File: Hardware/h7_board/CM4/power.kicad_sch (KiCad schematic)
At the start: 26 parts, among them IC4 TPS65133DPDR, IC5 TPS62111RSAT, J2 USB_C_Receptacle_USB2.0, Q1 AO3401A, U1 USBLC6-2SC6, U3 REF3433IDBVR

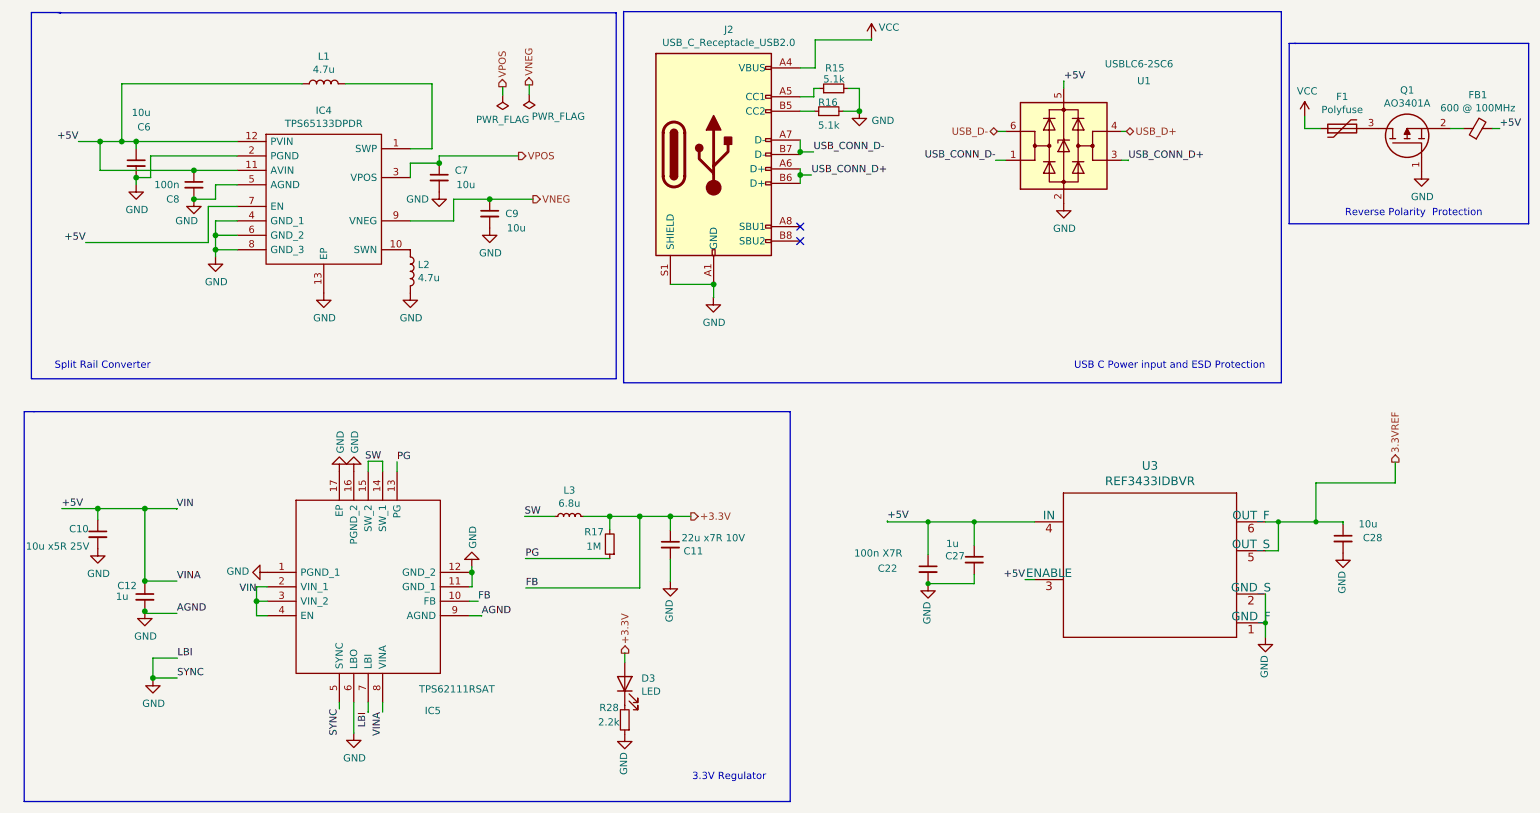
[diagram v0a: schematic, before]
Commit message: Edited Design to modify to LDO regulator and improve board layout
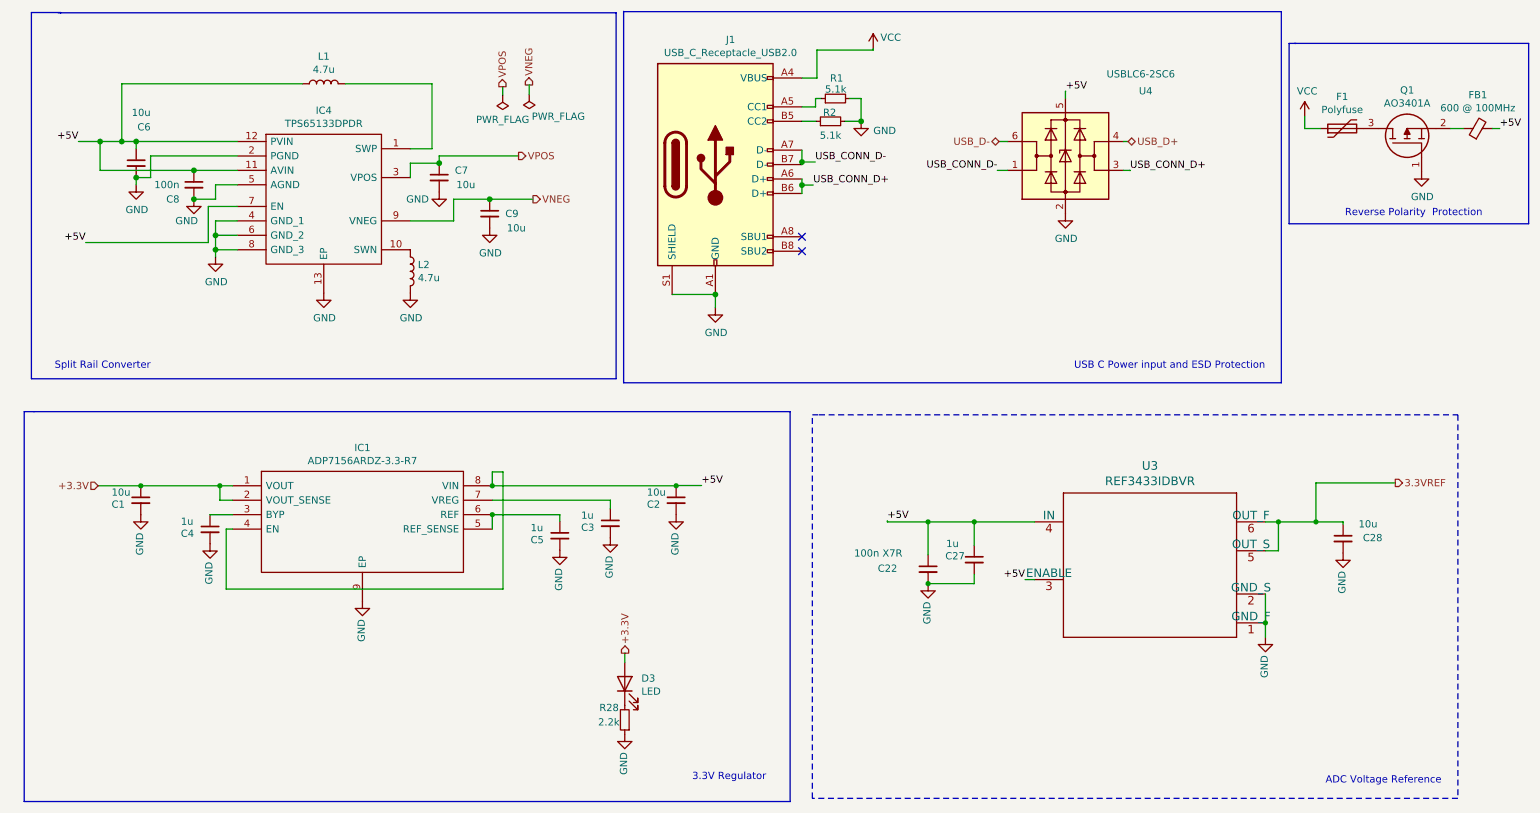
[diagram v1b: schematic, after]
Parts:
- removed C10: 10u x5R 25V, Capacitor_SMD:C_1210_3225Metric, symbol Device:C_Small
- removed C11: 22u x7R 10V, Capacitor_SMD:C_1210_3225Metric, symbol Device:C_Small
- removed C12: 1u, Capacitor_SMD:C_0805_2012Metric, symbol Device:C_Small
- removed IC5: TPS62111RSAT, SamacSys_Parts:QFN65P400X400X100-17N-D, symbol SamacSys_Parts:TPS62111RSAT
- removed J2: USB_C_Receptacle_USB2.0, CM4IO:TYPE-C-31-M-12, symbol Connector:USB_C_Receptacle_USB2.0
- removed L3: 6.8u, Inductor_SMD:L_TDK_SLF7032, symbol Device:L_Small
- removed R15, R16: 5.1k, Resistor_SMD:R_1206_3216Metric, symbol Device:R_Small
- removed R17: 1M, Resistor_SMD:R_0805_2012Metric, symbol Device:R_Small
- removed U1: USBLC6-2SC6, Package_TO_SOT_SMD:SOT-23-6, symbol Power_Protection:USBLC6-2SC6
- removed U3: REF3433IDBVR, footprints:REF3433IDBVR, symbol 2020-12-07_21-32-03:REF3433IDBVR
- added C1, C2: 10u, Capacitor_SMD:C_0603_1608Metric, symbol Device:C_Small
- added C3, C4, C5: 1u, Capacitor_SMD:C_0603_1608Metric, symbol Device:C_Small
- added IC1: ADP7156ARDZ-3.3-R7, SamacSys_Parts:SOIC127P600X175-9N, symbol SamacSys_Parts:ADP7156ARDZ-3.3-R7
- added J1: USB_C_Receptacle_USB2.0, CM4IO:TYPE-C-31-M-12, symbol Connector:USB_C_Receptacle_USB2.0
- added R1, R2: 5.1k, Resistor_SMD:R_1206_3216Metric, symbol Device:R_Small
- added U3: REF3433IDBVR, REF3433:REF3433IDBVR, symbol REF3433DBVR:REF3433IDBVR
- added U4: USBLC6-2SC6, Package_TO_SOT_SMD:SOT-23-6, symbol Power_Protection:USBLC6-2SC6
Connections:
- net +3.3V: now also C1.1, IC1.1 (VOUT), IC1.2 (VOUT_SENSE)
- net +5V: now also C2.1, IC1.4 (EN), IC1.8 (VIN), U3.3 (ENABLE), U3.4 (IN), U4.5 (VBUS)
- net 3.3VREF: now also U3.5 (OUT_S), U3.6 (OUT_F)
- net GND: now also C1.2, C2.2, C3.2, C4.2, C5.2, IC1.9 (EP), J1.A1 (GND), J1.A12 (GND), J1.B1 (GND), J1.B12 (GND), J1.S1 (SHIELD), R1.2, R2.2, U3.1 (GND_F), U3.2 (GND_S), U4.2 (GND)
- net USB_CONN_D+: now also J1.A6 (D+), J1.B6 (D+), U4.3 (I/O2)
- net USB_CONN_D-: now also J1.A7 (D-), J1.B7 (D-), U4.1 (I/O1)
- net USB_D+: now also U4.4 (I/O2)
- net USB_D-: now also U4.6 (I/O1)
- net VCC: now also J1.A4 (VBUS), J1.A9 (VBUS), J1.B4 (VBUS), J1.B9 (VBUS)
- new net: C3.1, IC1.7 (VREG)
- new net: J1.A5 (CC1), R1.1
- new net: C5.1, IC1.5 (REF_SENSE), IC1.6 (REF)
- new net: J1.B5 (CC2), R2.1
- new net: C4.1, IC1.3 (BYP)
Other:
- note added: "ADC Voltage Reference"

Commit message: Added Low noise analysis and design files
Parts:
- C1, C2: LCSC Part # C15849 -> C19702
- J1: LCSC Part # (none) -> C165948
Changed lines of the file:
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@@
   (junction (at 237.0328 103.7844) (diameter 0.9144) (color 0 0 0 0))
   (junction (at 243.6368 103.7844) (diameter 0.9144) (color 0 0 0 0))
+  (no_connect (at 153.162 56.134))
   (no_connect (at 153.162 53.594))
-  (no_connect (at 153.162 56.134))
   (wire (pts (xy 25.8064 36.83) (xy 29.6164 36.83))
     (stroke (width 0) (type solid) (color 0 0 0 0))
@@
       (effects (font (size 1.27 1.27)) hide)
     )
-    (property "LCSC Part #" "C15849" (id 4) (at 36.7792 99.9744 0)
+    (property "LCSC Part #" "C19702" (id 4) (at 36.7792 99.9744 0)
       (effects (font (size 1.27 1.27)) hide)
     )
@@
       (effects (font (size 1.27 1.27)) hide)
     )
-    (property "LCSC Part #" "C15849" (id 4) (at 131.0132 99.9744 0)
+    (property "LCSC Part #" "C19702" (id 4) (at 131.0132 99.9744 0)
       (effects (font (size 1.27 1.27)) hide)
     )
@@
       (effects (font (size 1.27 1.27)) hide)
     )
+    (property "LCSC Part #" " C165948" (id 4) (at 137.922 40.894 0)
+      (effects (font (size 1.27 1.27)) hide)
+    )
